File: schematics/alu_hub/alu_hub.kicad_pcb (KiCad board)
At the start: 2 copper layers, 100 x 91.1 mm, 40 parts, among them U1 74LS574, U10 74LS02, U2 74LS245, U3 74LS02, U4 74LS181, U5 74LS181, U6 74LS574, U7 74LS245, U8 74LS245, U9 74LS02

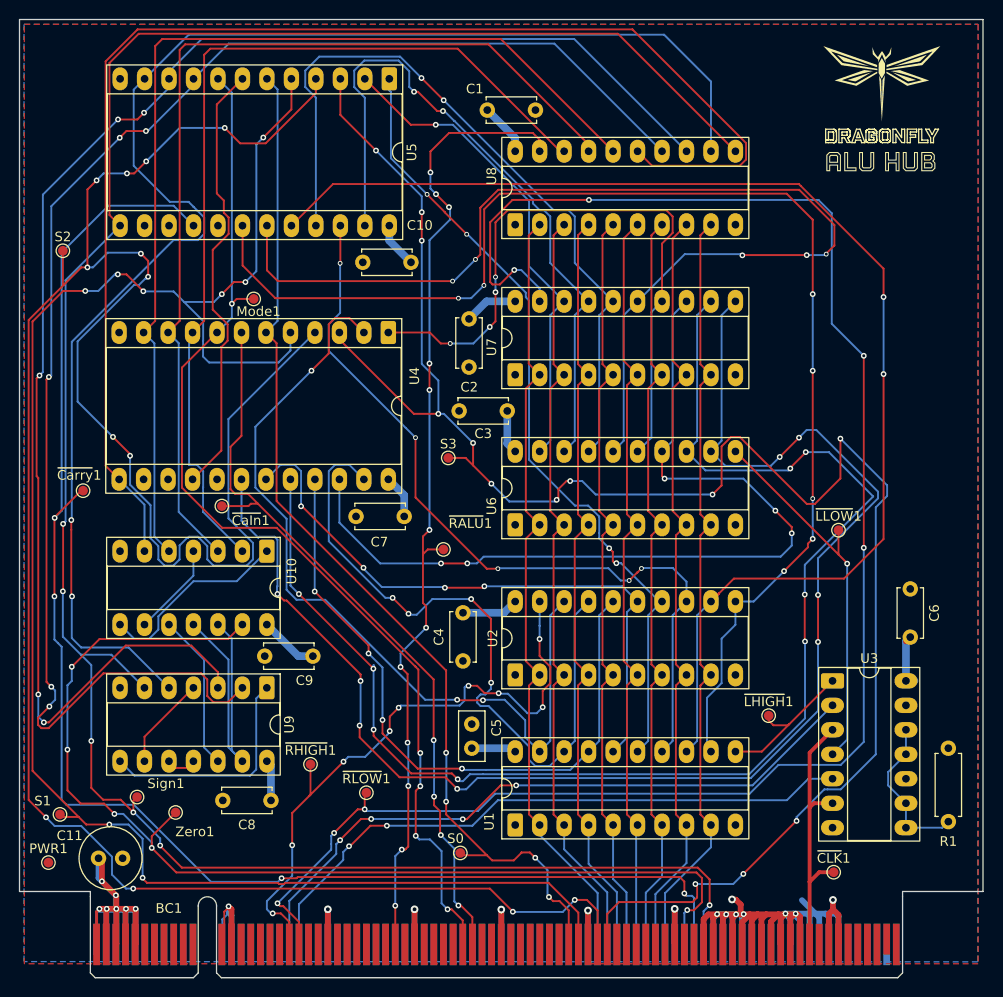
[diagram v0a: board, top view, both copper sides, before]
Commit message: fix(alu, interface): fix tp
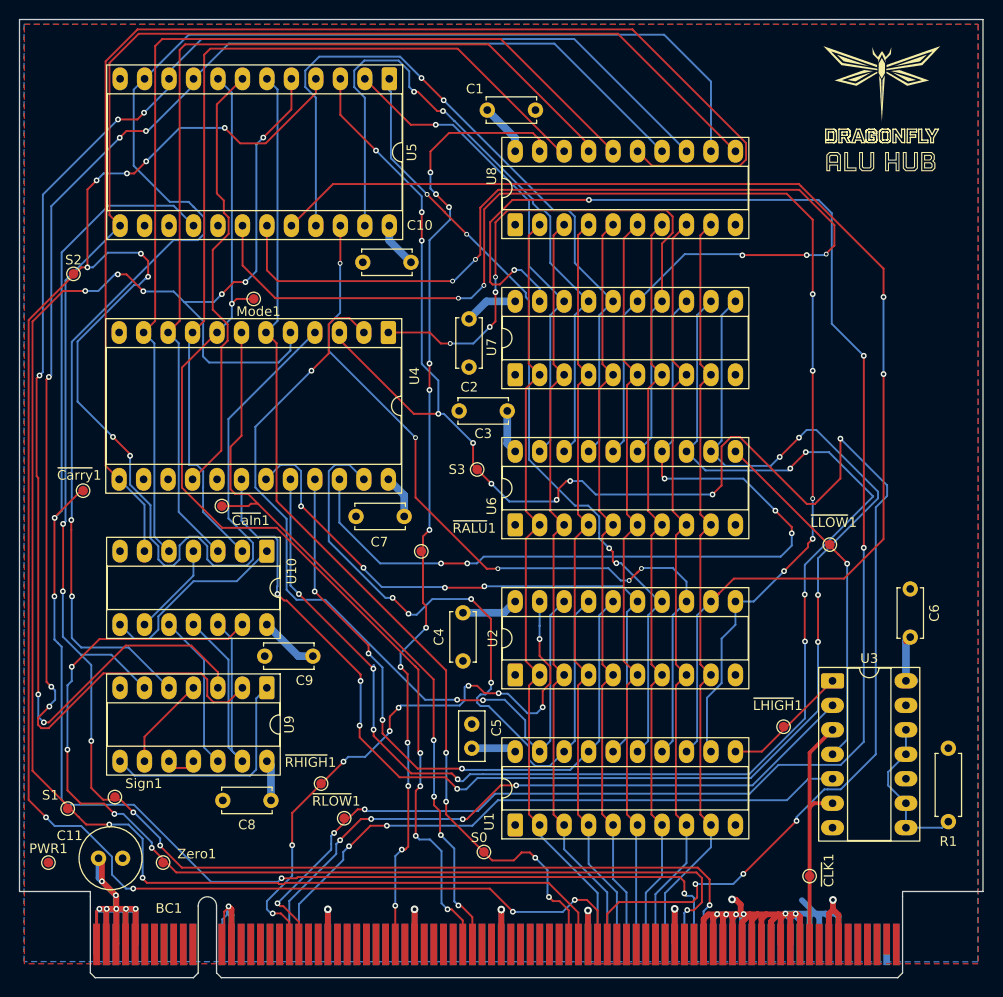
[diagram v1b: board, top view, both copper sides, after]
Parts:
- moved Zero1 5.36 mm to (114.9, 132.0)
- moved ~{RLOW}1 3.51 mm to (133.7, 127.4)
- moved S3 3.23 mm to (147.5, 91.2)
- moved S2 2.64 mm to (105.6, 70.9)
- moved ~{CLK}1 2.53 mm to (182.0, 133.4)
- moved S0 2.45 mm to (148.2, 130.9)
- moved ~{RALU}1 2.31 mm to (141.7, 99.7)
- moved Sign1 2.30 mm to (109.9, 125.2)
- moved ~{RHIGH}1 2.28 mm to (131.3, 123.8)
- moved ~{LHIGH}1 1.93 mm to (179.3, 117.9)
- moved ~{LLOW}1 1.75 mm to (184.1, 99.0)
- moved S1 1.00 mm to (105.0, 126.4)
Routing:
- net Net-(BC1-ALUZO): track 115.3 -> 110.6 mm
- net Net-(BC1-ALUS2): track 257.9 -> 254.3 mm
- net Net-(BC1-~{RARGH}): track 66.1 -> 62.7 mm
- net Net-(BC1-~{CLK}): track 28.8 -> 25.8 mm
- net Net-(BC1-ALUS3): track 192.4 -> 189.5 mm
- net Net-(BC1-ALUS0): track 110.6 -> 107.7 mm
- net Net-(U1-Cp): track 16.0 -> 13.3 mm
- net Net-(U6-Cp): track 39.4 -> 36.9 mm
- net Net-(BC1-~{RALU}): track 102.6 -> 100.3 mm
- net Net-(BC1-ALUS1): track 184.7 -> 182.6 mm
- net Net-(BC1-~{RARGL}): track 183.4 -> 181.6 mm
- net Net-(BC1-ALUSO): track 236.0 -> 234.3 mm

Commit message: final review
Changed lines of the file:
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@@
 		(tags "test point SMD pad")
 		(property "Reference" "~{CLK}1"
-			(at 2 -0.6 270)
+			(at 3 0 0)
 			(layer "F.SilkS")
 			(effects
@@
 		(tags "test point SMD pad")
 		(property "Reference" "S1"
-			(at -1.8 -1.4 0)
+			(at -1.75 -0.4 0)
 			(layer "F.SilkS")
 			(effects
@@
 		)
 		(fp_text user "${REFERENCE}"
-			(at -1.8 -1.402 0)
+			(at -1.75 -0.15 0)
 			(layer "F.Fab")
 			(effects
@@
 		(tags "test point SMD pad")
 		(property "Reference" "~{LHIGH}1"
-			(at -0.6 -2.2 0)
+			(at -1.3 -2.15 0)
 			(layer "F.SilkS")
 			(effects
@@
 		(tags "THT DIP DIL PDIP 2.54mm 7.62mm 300mil Socket LongPads")
 		(property "Reference" "U2"
-			(at 3.81 -2.33 90)
+			(at 1.5237 -3.195 90)
 			(layer "F.SilkS")
 			(effects
@@
 		(tags "test point SMD pad")
 		(property "Reference" "~{RLOW}1"
-			(at -0.825 -1.773 0)
+			(at 0.55 -1.9 0)
 			(layer "F.SilkS")
 			(effects
@@
 		(tags "test point SMD pad")
 		(property "Reference" "~{LLOW}1"
-			(at 0.4 -2.3 0)
+			(at 0.9 -2.25 0)
 			(layer "F.SilkS")
 			(effects
@@
 	)
 	(segment
+		(start 135.5 126.475)
+		(end 134.625 126.475)
+		(width 0.2)
+		(layer "F.Cu")
+		(net 38)
+	)
+	(segment
 		(start 129 138.15)
 		(end 127.375 136.525)
@@
 	)
 	(segment
-		(start 132.65 128.925)
-		(end 135.1 126.475)
+		(start 134.625 126.475)
+		(end 132.65 128.45)
 		(width 0.2)
 		(layer "F.Cu")
@@
 	)
 	(segment
-		(start 135.1 126.475)
-		(end 135.825 126.475)
-		(width 0.2)
-		(layer "F.Cu")
-		(net 38)
-	)
-	(segment
 		(start 127.075 136.525)
 		(end 126.775 136.225)
@@
 	)
 	(via
-		(at 135.825 126.475)
+		(at 135.5 126.475)
 		(size 0.6)
 		(drill 0.3)
@@
 	)
 	(via
-		(at 132.65 128.925)
+		(at 132.65 128.45)
 		(size 0.6)
 		(drill 0.3)
@@
 	)
 	(segment
-		(start 136.001 126.651)
-		(end 147.571943 126.651)
+		(start 132.65 128.45)
+		(end 132.35 128.75)
 		(width 0.2)
 		(layer "B.Cu")
@@
 	)
 	(segment
-		(start 132.35 130.65)
-		(end 132.35 130.075)
+		(start 147.747943 126.475)
+		(end 149.371943 124.851)
 		(width 0.2)
 		(layer "B.Cu")
@@
 	)
 	(segment
-		(start 187.625 119.472049)
-		(end 187.625 99.325)
+		(start 132.35 130.65)
+		(end 126.775 136.225)
 		(width 0.2)
 		(layer "B.Cu")
@@
 	)
 	(segment
-		(start 147.571943 126.651)
-		(end 149.371943 124.851)
+		(start 149.371943 124.851)
+		(end 175.7761 124.851)
 		(width 0.2)
 		(layer "B.Cu")
@@
 	)
 	(segment
-		(start 185.236049 121.861)
-		(end 187.625 119.472049)
+		(start 184.3 64.6)
+		(end 184.3 76.075)
 		(width 0.2)
 		(layer "B.Cu")
@@
 	)
 	(segment
-		(start 184.3 64.6)
-		(end 184.3 76.075)
+		(start 178.7661 121.861)
+		(end 185.236049 121.861)
 		(width 0.2)
 		(layer "B.Cu")
@@
 	)
 	(segment
-		(start 149.371943 124.851)
-		(end 175.7761 124.851)
-		(width 0.2)
-		(layer "B.Cu")
-		(net 38)
-	)
-	(segment
 		(start 152.075 70.5)
 		(end 153.985 72.41)
@@
 	)
 	(segment
-		(start 135.825 126.475)
-		(end 136.001 126.651)
+		(start 135.5 126.475)
+		(end 147.747943 126.475)
 		(width 0.2)
 		(layer "B.Cu")
@@
 	)
 	(segment
-		(start 132.35 129.225)
-		(end 132.65 128.925)
+		(start 185.236049 121.861)
+		(end 187.625 119.472049)
 		(width 0.2)
 		(layer "B.Cu")
@@
 	)
 	(segment
-		(start 175.7761 124.851)
-		(end 178.7661 121.861)
-		(width 0.2)
-		(layer "B.Cu")
-		(net 38)
-	)
-	(segment
-		(start 132.35 130.075)
-		(end 132.35 129.225)
+		(start 132.35 128.75)
+		(end 132.35 130.65)
 		(width 0.2)
 		(layer "B.Cu")
@@
 	)
 	(segment
-		(start 126.775 136.225)
-		(end 132.35 130.65)
+		(start 187.625 119.472049)
+		(end 187.625 99.325)
 		(width 0.2)
 		(layer "B.Cu")
@@
 	)
 	(segment
-		(start 178.7661 121.861)
-		(end 185.236049 121.861)
+		(start 175.7761 124.851)
+		(end 178.7661 121.861)
 		(width 0.2)
 		(layer "B.Cu")
